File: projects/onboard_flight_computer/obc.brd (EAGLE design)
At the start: 90.2 x 95.9 mm, 191 parts, among them IC1 IS42S16160J-6BLI, IC2 S26KS512SDPBHI020, IC3 74LVC2T45GS,115, IC4 74LVCH1T45GS,132, IC5 MIMXRT1052DVJ6B, IC7 74LVCH1T45GS,132, IC8 74LVCH1T45GS,132, J1 504050-0791, J2 DX4R205JJAR1800, J3 504050-0791, J4 504050-0791, J5 504050-0791, J6 ESQ-126-37-G-D, J7 FH28-10S-0.5SH_05_, J8 504050-1091, J9 ESQ-126-37-G-D, Q1 FA-128, Q3 FC-12M, U10 HONEYWELL_HMC5983-TRHONEYWELL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, U11 HONEYWELL_HMC5983-TRHONEYWELL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, U12 HONEYWELL_HMC5983-TRHONEYWELL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, U13 DS1307N, U2 MCP1702T-1802E/CB, U3 NXP_FXAS21002CQR1NXP_FXAS2100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, U4 MK20DX128VFM5, U5 NLX2G14CMUTCG, U6 NTSX2102GU8H, U7 NXP_FXAS21002CQR1NXP_FXAS2100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, U8 NX5P3090UKZ, U9 NXP_FXAS21002CQR1NXP_FXAS2100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, Y1 ECS-.327-12.5-13X

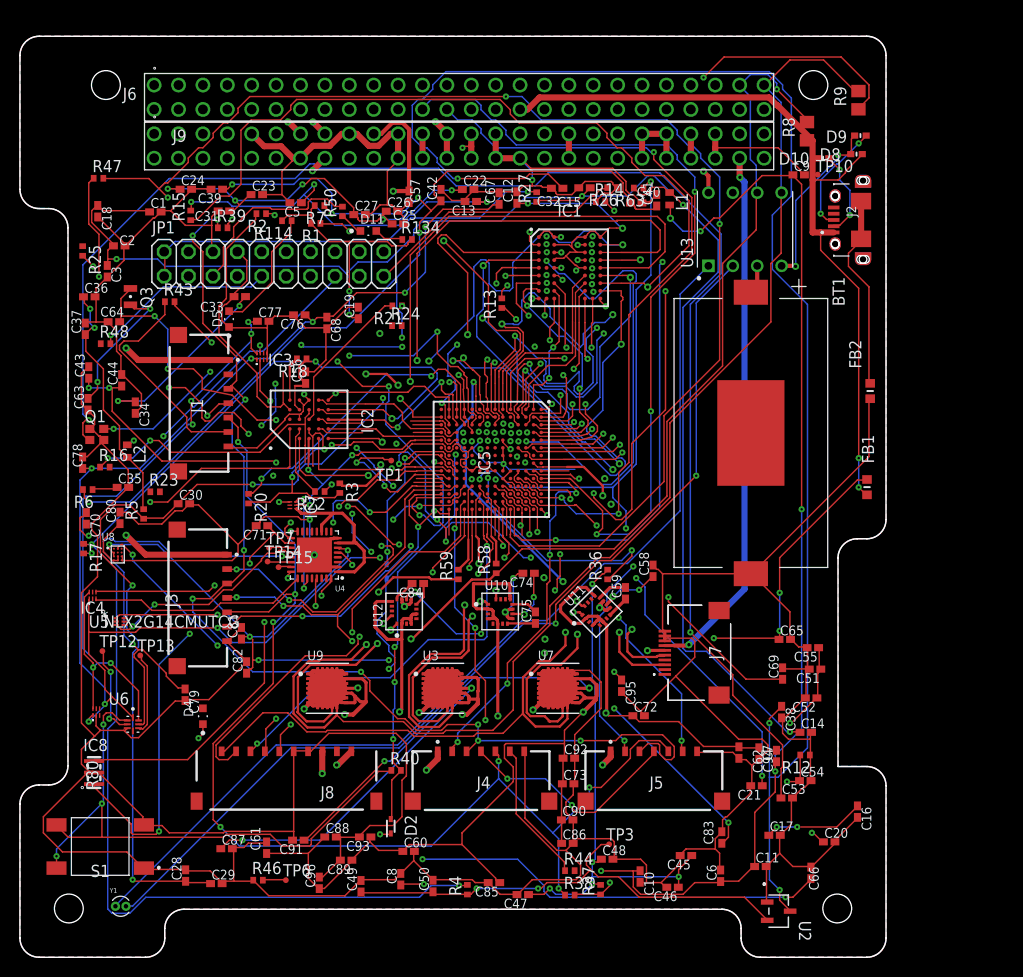
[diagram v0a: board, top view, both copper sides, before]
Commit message: RT1020 libraries added, OBC routed for RT1020
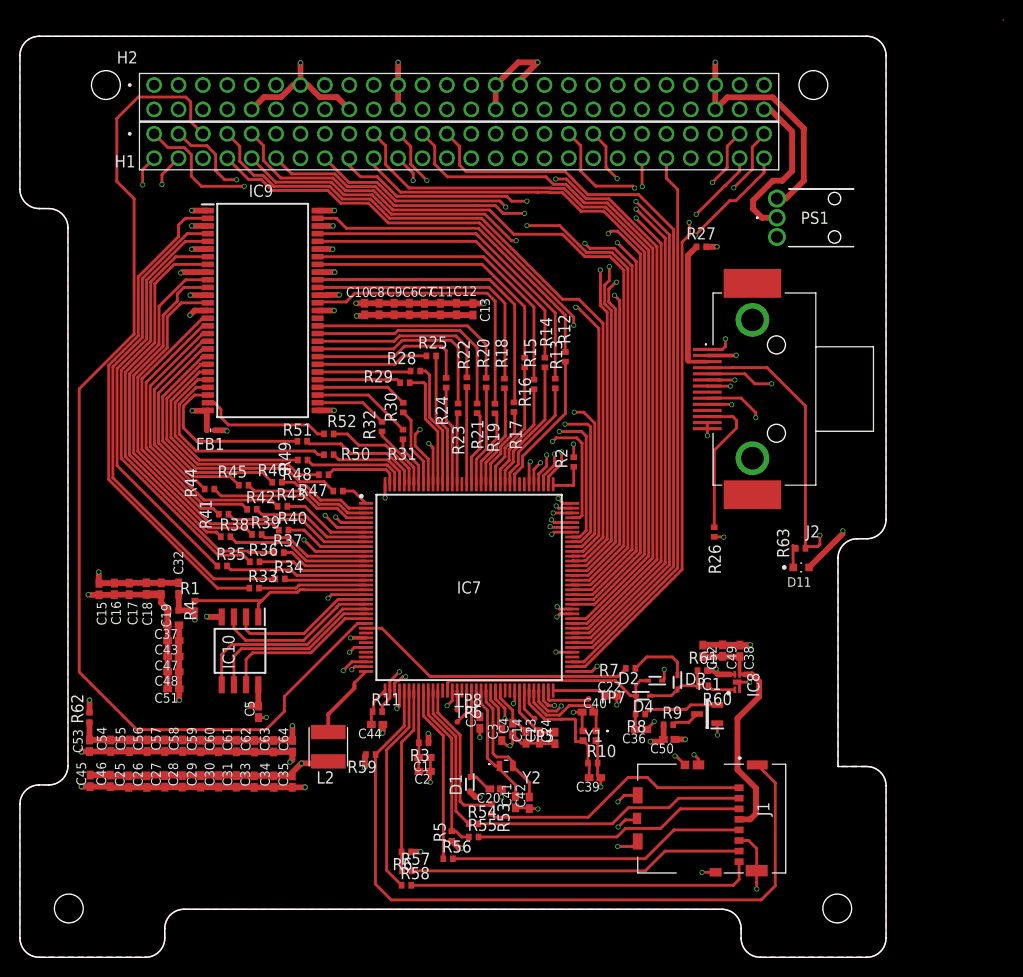
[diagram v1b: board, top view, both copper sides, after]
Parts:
- removed BT1: BA2032SM, BA2032SM:BAT_BA2032SM
- removed C65, C69, C82: 10 uF, rcl:C0402K
- removed C66: 2.2 uF, rcl:C0402K
- removed C67, C72, C73, C76, C77, C78, C81, C85, C88, C89, C92, C93, C96: 0.1 uF, rcl:C0402K
- removed C68, C86, C90, C94: 1.0 uF, rcl:C0402K
- removed C70, C71: 22 pF, rcl:C0402K
- removed C74, C80, C83: 4.7 uF, rcl:C0402K
- removed C75, C84: 0.22 uF, rcl:C0402K
- removed C79: 1000 pF, rcl:C0402K
- removed C87, C91, C95: 100 nF, rcl:C0402K
- removed D10, D8, D9: 0402ESDA-MLP1, 0402ESDA-MLP1:DIONC1105X44N
- removed D5: KINGBRIGHT_KPT-1608SGCKINGBRIGHT_KPT-1608SGC_0_0, Kingbright - KPT-1608SGC:KINGBRIGHT_KPT-1608SGC_0
- removed D6: RB521S30T1G, RB521S30T1G:SODFL1608X70N
- removed FB2: MPZ1608S331A, MPZ1608S331A:BEADC1608X95N
- removed IC2: S26KS512SDPBHI020, SDRAM_and_HyperFlash:BGA24C100P5X5_600X800X100
- removed IC3: 74LVC2T45GS,115, 74LVC2T45GS_115:74AXP2T3407GSX
- removed IC4: 74LVCH1T45GS,132, 74LVCH1T45GS_132:74LVC1G3157GS132
- removed IC5: MIMXRT1052DVJ6B, MIMXRT1052DVJ6B:BGA196C80P14X14_1200X1200X161
- removed J3, J4, J5: 504050-0791, 504050-0791:504050-0791
- removed J6, J9: ESQ-126-37-G-D, ESQ-126-37-G-D:ESQ-126-Y-X
- removed J7: FH28-10S-0.5SH_05_, FH28-10S-0.5SH_05_:FH2810S05SH05
- removed J8: 504050-1091, 504050-1091:504050-1091
- removed JP1: 20, pinhead:2X10
- removed L1: 120 Ohm, inductors:0402
- removed Q1: FA-128, crystal:FA-128
- removed Q3: FC-12M, crystal:FC-12M
- removed R114, R134: 1k Ohm, rcl:R0402
- removed R80: CSTCE8M00G55-R0, CSTCE8M00G55-R0:CSTCE12M0G55-R0
- removed S1: TL3301AF260QG, TL3301AF260QG:TL3301AF260QG
- removed TP1, TP10, TP12, TP13, TP14, TP15, TP3: TPTP06R, testpad:TP06R
- removed U10, U11, U12: HONEYWELL_HMC5983-TRHONEYWELL_HMC5983-TR_0_0, Honeywell - HMC5983-TR:HONEYWELL_HMC5983-TR_0
- removed U13: DS1307N, DS1307N:DIP762W47P254L991H457Q8
- removed U2: MCP1702T-1802E/CB, MCP1702T1802ECB:SOT-23A_MC
- removed U3, U7, U9: NXP_FXAS21002CQR1NXP_FXAS21002CQR1_0_0, NXP - FXAS21002CQR1:NXP_FXAS21002CQR1_0
- removed U4: MK20DX128VFM5, MK20DX128VFM5:QFN50P500X500X100-33N
- removed U5: NLX2G14CMUTCG, NLX2G14CMUTCG:UDFN6_1X1
- removed U6: NTSX2102GU8H, NTSX2102GU8H:QFN40P140X120X50-8N
- removed U8: NX5P3090UKZ, NX5P3090UKZ:BGA12CP40_3X4_135X165X56B26N
- added C4: 0.1uF, rcl:C0402K
- added D1, D3: BAT54XV2T1G, BAT54XV2T1G:SODFL1608X70N
- added H1, H2: ESQ-126-39-G-D, ESQ-126-39-G-D:SAMTEC_ESQ-126-39-G-D
- added IC10: IS25LP064A-JBLE, IS25LP064A-JBLE:SOIC127P790X216-8N
- added IC9: IS42S16160J-6TL, IS42S16160J-6TL:SOP80P1176X120-54N
- added PS1: PJ-040D, PJ-040D:PJ040D
- added R10: 2.2M Ohm, rcl:R0402
- added R11: 30k Ohm, rcl:R0402
- added R19, R28, R29, R30, R31, R32, R33, R34, R35, R41, R42, R45, R49, R51, R52, R53, R54, R55, R56, R57, R60, R61, R62: 0 Ohm, rcl:R0402
- added TP5, TP8: TPTP06R, testpad:TP06R
- added Y2: ECS-.327-7-12-TR, ECS-.327-7-12-TR:ECS327712TR
- C14: value 0.22uF -> 10 uF
- C16, C19, C31, C33, C48: value 4.7uF -> 0.22uF
- C17, C23, C36: value 0.22uF -> 0.1uF
- C18, C24, C35: value 0.22uF -> 4.7uF
- C2, C51: value 0.1uF -> 4.7uF
- C3: value 4.7uF -> 1.0 uF
- C32, C43: value 10uF -> 0.1uF
- C37: value 33uF -> 0.1uF
- C39: value 4.7uF -> 4.7pF
- C40: value 0.22uF -> 4.7pF
- C41, C42: value 0.22uF -> 10pF
- C44, C45, C46, C47: value 0.1uF -> 0.22uF
- C5: value 22uF -> 1.0uF
- C50: value 0.1uF -> 1.0uF
- C52: value 4.7uF -> 1.0uF
- C53, C54, C55: value 4.7uF -> 0.1uF
- C57: value 0.1 uF -> 0.1uF
- C58: value 4.7 uF -> 0.1uF
- C59: value 0.22 uF -> 0.1uF
- C60, C61, C62: value 0.1 uF -> 4.7uF
- C63, C64: value 18pF -> 4.7uF
- D2: value RB521S30T1G -> BAT54XV2T1G; device RB521S30T1G:SODFL1608X70N -> BAT54XV2T1G:SODFL1608X70N
- D4: value KINGBRIGHT_KPT-1608SGCKINGBRIGHT_KPT-1608SGC_0_0 -> BAT54XV2T1G; device Kingbright - KPT-1608SGC:KINGBRIGHT_KPT-1608SGC_0 -> BAT54XV2T1G:SODFL1608X70N
- FB1: value MPZ1608S331A -> BLM15AG121SN1D; device MPZ1608S331A:BEADC1608X95N -> BLM15AG121SN1D:NFZ15SG152SN10B
- IC1: value IS42S16160J-6BLI -> TPS3839L30DBZR; device SDRAM_and_HyperFlash:BGA54C80P9X9_800X800X120 -> TPS3839L30DBZR:SOT95P237X112-3N
- IC7: value 74LVCH1T45GS,132 -> MIMXRT1021DAG5A; device 74LVCH1T45GS_132:74LVC1G3157GS132 -> MIMXRT1021DAG5A:QFP50P2200X2200X160-144N
- IC8: value 74LVCH1T45GS,132 -> MIC94305YMT-TR; device 74LVCH1T45GS_132:74LVC1G3157GS132 -> MIC94305YMT-TR:SON50P160X120X60-5N
- J1: value 504050-0791 -> 504077-1891; device 504050-0791:504050-0791 -> 504077-1891:5040771891
- J2: value DX4R205JJAR1800 -> 12214-8250-00FR; device DX4R205JJAR1800:JAE_DX4R205JJAR1800 -> 12214-8250-00FR:12214825000FR
- L2: value 4.7 uH -> SRN4026-4R7M; device inductors:0402 -> SRN4026-4R7M:SRN4026
- R1, R5, R59: value 0 Ohm -> 10k Ohm
- R12: value 2.2M Ohm -> 0 Ohm
- R14, R15: value 100K Ohm -> 0 Ohm
- R17, R18, R3: value 10k Ohm -> 0 Ohm
- R26: value 10k Ohm -> 100 Ohm
- R36, R37: value 4.7K Ohm -> 0 Ohm
- R46: value 10K Ohm -> 0 Ohm
- R6: value 30K Ohm -> 10k Ohm
- R8: value 4.7 k -> 0 Ohm; device rcl:R0805 -> rcl:R0402
- R9: value 4.7k -> 1k Ohm; device rcl:R0805 -> rcl:R0402
- Y1: value ECS-.327-12.5-13X -> XRCGB24M000F2P01R0; device ECS-.327-12.5-13X:XTAL_ECS-.327-12.5-13X -> XRCGB24M000F2P01R0:XRCGB24M000F2P01R0
- moved C16 80.8 mm to (9.83, 38.4)
- moved C36 73.0 mm to (64.7, 23.7), turned to 180 degrees
- moved C39 72.8 mm to (59.9, 18.7)
- moved C53 72.8 mm to (7.24, 22.0), turned to 90 degrees
- moved C54 72.4 mm to (9.45, 22.0), turned to 90 degrees
- moved C17 71.9 mm to (11.4, 38.4), turned to 270 degrees
- moved C55 71.9 mm to (11.4, 22.0), turned to 90 degrees
- moved C24 68.8 mm to (55.7, 22.8), turned to 90 degrees
- moved FB1 68.6 mm to (19.9, 54.9), turned to 180 degrees
- moved R9 68.0 mm to (67.5, 24.2), turned to 0 degrees
- moved C6 67.3 mm to (40.5, 67.5)
- moved C11 66.9 mm to (43.8, 67.5), turned to 90 degrees
- moved C51 66.8 mm to (16.0, 27.9)
- moved IC8 66.8 mm to (74.7, 28.7), turned to 90 degrees
- moved J1 66.1 mm to (72.0, 14.8), turned to 270 degrees
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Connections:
- removed net 12V_BUS: J9.23, J9.24
- removed net 12V_PDM1: J9.8
- removed net 12V_PDM2: J9.10
- removed net 3V3_PDM10: J9.20
- removed net 3V3_PDM8: J9.18
- removed net 3V3_PDM9: C57.1, C60.1, C61.1, C62.1, C72.1, C73.1, C85.1, C86.1, C88.1, C89.1, C90.1, C92.1, C93.1, C94.1, C96.1, J7.6, J9.19, U10.13, U10.2, U10.4, U10.6, U11.13, U11.2, U11.4, U11.6, U12.13, U12.2, U12.4, U12.6, U3.13, U3.15, U3.17, U3.18, U7.13, U7.15, U7.17, U7.18, U9.13, U9.15, U9.17, U9.18
- removed net 5V_BUS: J9.25, J9.26, R8.1, R9.1, U13.8
- removed net 5V_PDM5: J8.3, J9.13
- removed net 5V_PDM6: J1.1, J3.1, J4.1, J5.1, J9.15
- removed net 5V_PDM7: J8.1, J9.16
- removed net 5V_USB_CHARGE: D8.2, FB1.1, J2.1, J6.32
- removed net AAA: U8.A1
- removed net BATV_BUS: J9.45, J9.46
- removed net BATV_PDM3: J9.11
- removed net BATV_PDM4: J9.12
- removed net BCR_OUT: J9.41, J9.42, J9.43, J9.44
- removed net CAN_STBY: IC5.G14, R44.2
- removed net CHASSIS: J7.7, J9.50
- removed net DCDC_3V3: C1.1, C14.1, C15.1, C18.1, C19.1, C2.1, C3.1, D6.2, IC5.E6, IC5.F5, IC5.N14, IC5.P12, L1.1, R1.2, R114.2, R134.2, R27.1, R63.2, R7.2
- removed net FLASH_RST: IC5.D7, R2.1
- removed net FLASH_VCC: C51.1, C52.1, C55.1, C56.1, IC2.B4, IC2.D1, IC2.E4, IC5.K5, R17.1, R18.1, R3.1, R4.2
- removed net FLEXSPI_CLK_B: IC2.B1, IC5.P2
- removed net FLEXSPI_D0_B: IC2.D5, IC5.M4
- removed net FLEXSPI_D1_B: IC2.E3, IC5.M3
- removed net FLEXSPI_D2_B: IC2.E2, IC5.M5
- removed net FLEXSPI_D3_B: IC2.E1, IC5.L5
- removed net FLEXSPI_DQS: IC5.N3, R21.1
- removed net GPIO_AD_B1_00: IC5.J11, R58.2
- removed net GPIO_AD_B1_01: IC5.K11, R59.2
- removed net LDO_1V8: C49.1, C50.1, R4.1, TP3.TP, U2.2
- removed net MCU_DCDC_IN: C39.1, C40.1, C41.1, C42.1, IC5.K4, IC5.L1, IC5.L2, R6.2, R7.1
- removed net N$27: IC2.A5, R18.2
- removed net N$29: IC2.A4, R2.2
- removed net N$31: IC2.C2, R20.2, R3.2
- removed net N$34: IC2.B2, R22.2
- removed net N$37: JP1.19, R26.2
- removed net N$39: D2.1, JP1.15
- removed net N$40: C32.1, C38.1, R1.1, U2.3
- removed net N$46: C75.1, U10.8
- removed net N$48: C59.1, U11.8
- removed net N$49: C84.2, U12.12
- removed net N$53: C63.2, IC5.N9, Q3.2
- removed net N$54: U6.5
- removed net N$56: C83.1, U12.10
- removed net N$57: TP12.TP, U6.3
- removed net N$60: TP13.TP, U6.6
- removed net N$67: C91.1, U7.16
- removed net N$71: C87.1, U3.16
- removed net N$72: C95.1, U9.16
- removed net N$76: D11.2, R134.1
- removed net P3V3_SDA: C67.1, C68.1, C69.1, C76.1, C78.1, IC3.1, IC4.1, IC7.1, IC8.1, U4.1, U4.11, U4.7, U5.5, U6.1
- removed net P5V_SDA: C65.1, C81.1, C82.1, FB1.2, U4.6, U8.B1, U8.B2, U8.C1
- removed net P5V_SDA_S: C80.1, U8.C2, U8.D1, U8.D2
- removed net PCM_IN: J9.35, J9.36
- removed net POWER_EN: U4.31
- removed net POWER_LED: D5.2, R114.1
- removed net SDA_EXTAL: C70.1, R80.3, U4.17
- removed net SDA_LED: D4.1, U4.29
- removed net SDA_RST: TP7.TP, U4.19
- removed net SDA_RST_TGTMCU_B: C79.1, R40.1, S1.2, S1.4, U4.21, U6.2, U6.7
- removed net SDA_RX_EN: IC4.5
- removed net SDA_SPI0_CS: TP15.TP, U4.23
- removed net SDA_SPI0_RST_B: TP14.TP, U4.22
- removed net SDA_SPI0_SCK: IC8.3, U4.26
- removed net SDA_SPI0_SIN: IC3.3, U4.28
- removed net SDA_SPI0_SOUT: IC7.3, U4.27
- removed net SDA_SWD_EN: IC8.5, U5.6
- removed net SDA_SWD_EN_B: U4.16, U5.1
- removed net SDA_SWD_OE: IC7.5, U5.4
- removed net SDA_SWD_OE_B: U4.20, U5.3
- removed net SDA_USBSHIELD: FB2.2, J2.S4, J2.S5
- removed net SDA_USB_CONN_DN: D10.2, J2.2
- removed net SDA_USB_CONN_DP: D9.2, J2.3
- removed net SDA_USB_DN: U4.4
- removed net SDA_USB_DP: U4.3
- removed net SDA_VOUT33: C66.1, U4.5
- removed net SDA_XTAL: C71.1, R80.1, U4.18
- removed net SPI1_EN_1: IC5.A9, J1.2
- removed net SPI1_EN_2: IC5.B9, J3.2
- removed net SPI1_EN_3: IC5.C9, J4.2
- removed net SPI1_EN_4: IC5.D9, J5.2
- removed net SPI1_NSS_1: J1.6, R43.1
- removed net SPI1_NSS_2: IC5.F11, J3.6
- removed net SPI1_NSS_3: J4.6, R44.1
- removed net SPI1_NSS_4: IC5.H14, J5.6
- removed net SWD_CLK: IC8.4, R48.1
- removed net SWD_DIO: IC3.6, IC7.4, R47.1
- removed net TC_SDA_USB_ID_TP: J2.4, TP10.TP
- removed net UART1_RXD: IC4.4, IC5.L14
- removed net UART1_RX_TGTMCU_R: IC4.3, U4.25
- removed net UART1_TXD: IC3.7, IC5.K14
- removed net UART1_TX_TGTMCU_R: IC3.2, U4.24
- removed net UART2_RX: IC5.M12, J6.3
- removed net UART2_TX: IC5.L11, J6.1
- removed net UART8_RX: IC5.J13, J8.8
- removed net UART8_TX: IC5.L13, J8.7
- removed net USB_OTG1_ID: IC5.H10, R36.1, R39.2
- removed net USB_OTG1_OC: IC5.G11, R43.2
- removed net VDD_SOC_IN: C22.1, C23.1, C24.1, C25.1, C26.1, C27.1, C28.1, C29.1, C30.1, C31.1, IC5.F6, IC5.F7, IC5.F8, IC5.F9, IC5.J5, R5.1
- removed net VTRG_FAULT_B: U4.32, U8.A2
- removed net V_TGTMCU: C77.1, IC3.8, IC4.6, IC7.6, IC8.6, U6.8
- new net 5V_USB: H2.52, PS1.1
- new net 5V_USB_OTG: C3.2, IC7.59
- new net FLASH_3V3: C32.2, C5.2, IC10.8, R1.1, R4.2
- new net GPANAIO: IC7.71, TP7.TP
- new net GPIO_EMC_16: IC9.23, R49.1
- new net GPIO_EMC_17: IC9.24, R50.1
- new net GPIO_EMC_18: IC9.25, R51.1
- new net GPIO_EMC_19: IC9.26, R52.1
- new net GPIO_EMC_20: IC9.29, R32.2
- new net GPIO_EMC_21: IC9.30, R31.2
- new net GPIO_EMC_22: IC9.31, R30.2
- new net GPIO_EMC_23: IC9.32, R29.2
- new net GPIO_EMC_24: IC9.33, R28.2
- new net GPIO_EMC_25: IC9.34, R25.2
- new net GPIO_EMC_26: IC9.35, R24.2
- new net GPIO_EMC_27: IC9.36, R23.2
- new net INT1_COMBO: IC7.27, R7.1
- new net JTAG_DACK: J2.13, R26.1
- new net JTAG_NSRST: D2.1, J2.12
- new net N$12: IC9.11, R39.1
- new net N$14: IC9.13, R40.1
- new net N$15: J1.5, R56.2
- new net N$16: IC9.15, R41.1
- new net N$17: IC9.16, R42.1
- new net N$18: IC9.17, R43.1
- new net N$19: IC9.18, R44.1
- new net N$20: IC9.19, R45.1
- new net N$21: IC9.20, R46.1
- new net N$22: IC9.21, R47.1
- new net N$23: IC9.22, R48.1
- new net N$24: D3.2, D4.2, R60.1, R61.1
- new net N$25: J1.7, R57.2
- new net N$42: IC9.47, R16.2
- new net NVCC_PLL: C22.2, IC7.72
- new net NVCC_SD0: C1.2, C2.2, IC7.44, R3.2
- new net PMIC_STBY_REQ: IC7.54, TP6.TP
- new net RTC_XTALI: C41.2, IC7.57, Y2.1
- new net SD1_CLK: IC7.45, R56.1
- new net SD1_CMD: IC7.46, R5.2, R55.1
- new net SD1_D0: IC7.43, R57.1, R6.2
- new net SD1_D1: IC7.42, R58.1
- new net SD1_D2: IC7.48, R53.1
- new net SD1_D3: IC7.47, R54.1
- new net SD_CD_SW: IC7.41, J1.9, R59.1
- new net SD_PWREN: D3.1, R7.2
- new net SPI1_EN0: H1.9, IC7.92
- new net SPI1_EN1: H1.10, IC7.91
- new net SPI1_EN2: H1.22, IC7.90
- new net SPI1_EN3: H1.21, IC7.89
- new net SPI1_PCS0: H1.7, IC7.97
- new net SPI1_PCS1: H1.8, IC7.88
- new net SPI1_PCS2: H1.20, IC7.87
- new net SPI1_PCS3: H1.19, IC7.84
- new net UART1_RX: H1.4, IC7.101
- new net UART1_TX: H1.2, IC7.105
- new net UART4_RX: H1.3, IC7.79
- new net UART4_TX: H1.1, IC7.80
- new net USB_OTG1_CHD: IC7.66, TP5.TP
- new net VDD_HIGH_CAP: C23.2, C24.2, IC7.65
- new net VDD_SNVS_CAP: C21.2, IC7.56
- new net VSD_3V3: C38.2, C49.2, C52.2, IC8.3, J1.4
- new net WAKEUP: IC7.52, TP8.TP
- new net XTALO: C40.2, IC7.68, Y1.1
- net 3V3_BUS: now also C15.2, C16.2, C17.2, C18.2, C19.2, C37.2, C43.2, C47.2, C48.2, C50.2, C51.2, D1.2, D11.2, FB1.1, H2.27, H2.28, IC7.34, IC7.38, IC7.69, IC7.73, IC8.4, J2.8, R11.2, R27.2, R3.1, R4.1, R5.1, R59.2, R6.1, R61.2, R62.2, R9.1; no longer IC5.J6, J9.27, J9.28
- net ANT_BURN_WIRE1: now also H1.23, IC7.83; no longer IC5.A10, J6.24
- net ANT_BURN_WIRE2: now also H1.25, IC7.78; no longer IC5.D10, J6.26
- net DCDC_OUT: now also C25.2, C26.2, C27.2, C28.2, C29.2, C30.2, C31.2, C33.2, C34.2, C35.2, C45.2, C46.2, IC7.102, IC7.114, IC7.134, IC7.31, IC7.39, IC7.5, IC7.86, L2.1; no longer C36.1, C37.1, L2.2, R5.2
- net DTR: now also H1.5, IC7.26; no longer IC5.C10, J8.6
- net FLEXSPI_CLK: now also IC10.6, IC7.24; no longer IC5.L4, R22.1
- net FLEXSPI_D0_A: now also IC10.5, IC7.23; no longer IC5.P3, R24.2
- net FLEXSPI_D1_A: now also IC10.2, IC7.21; no longer IC5.N4, R23.2
- net FLEXSPI_D2_A: now also IC10.3, IC7.22; no longer IC5.P4, R16.2
- net FLEXSPI_D3_A: now also IC10.7, IC7.25; no longer IC5.P5, R25.2
- net FLEXSPI_SS0: now also IC10.1, IC7.19, R1.2; no longer IC5.L3, R20.1
- net GND: now also C1.1, C14.1, C15.1, C16.1, C17.1, C18.1, C19.1, C2.1, C20.1, C21.1, C22.1, C23.1, C24.1, C25.1, C26.1, C27.1, C28.1, C29.1, C3.1, C30.1, C31.1, C32.1, C33.1, C34.1, C35.1, C36.1, C37.1, C38.1, C39.1, C4.1, C40.1, C41.1, C42.1, C43.1, C44.1, C45.1, C46.1, C47.1, C48.1, C49.1, C5.1, C50.1, C51.1, C52.1, C53.1, C54.1, C55.1, C56.1, C57.1, C58.1, C59.1, C60.1, C61.1, C62.1, H2.10, H2.13, H2.18, H2.21, H2.22, H2.29, H2.30, H2.31, H2.47, H2.48, IC1.1, IC10.4, IC7.103, IC7.113, IC7.135, IC7.35, IC7.40, IC7.51, IC7.6, IC7.60, IC7.64, IC7.70, IC7.85, IC8.5, IC9.12, IC9.28, IC9.41, IC9.46, IC9.52, IC9.54, IC9.6, J1.10, J1.11, J1.12, J1.13, J1.14, J1.15, J1.16, J1.6, J2.1, J2.14, J2.7, PS1.2, R10.2, R2.1, R26.2, Y1.2, Y1.4; no longer BT1.-, C1.2, C14.2, C15.2, C16.2, C17.2, C18.2, C19.2, C2.2, C20.2, C21.2, C22.2, C23.2, C24.2, C25.2, C26.2, C27.2, C28.2, C29.2, C3.2, C30.2, C31.2, C32.2, C33.2, C34.2, C35.2, C36.2, C37.2, C38.2, C39.2, C40.2, C41.2, C42.2, C43.2, C44.2, C45.2, C46.2, C47.2, C48.2, C49.2, C5.2, C50.2, C51.2, C52.2, C53.2, C54.2, C55.2, C56.2, C57.2, C58.2, C60.2, C61.2, C62.2, C65.2, C66.2, C67.2, C68.2, C69.2, C70.2, C71.2, C72.2, C73.2, C74.2, C76.2, C77.2, C78.2, C79.2, C80.2, C81.2, C82.2, C83.2, C85.2, C86.2, C87.2, C88.2, C89.2, C90.2, C91.2, C92.2, C93.2, C94.2, C95.2, C96.2, D10.1, D5.1, D8.1, D9.1, FB2.1, IC1.A1, IC1.A3, IC1.B7, IC1.C3, IC1.D7, IC1.E3, IC1.J1, IC2.B3, IC2.B5, IC2.C1, IC2.C5, IC2.E5, IC3.4, IC3.5, IC4.2, IC5.A1, IC5.A14, IC5.G9, IC5.K6, IC5.K9, IC5.N1, IC5.N2, IC7.2, J1.7, J2.5, J3.7, J4.7, J5.7, J7.10, J7.8, J7.9, J8.4, J8.5, J9.14, J9.17, J9.21, J9.22, J9.29, J9.30, J9.32, J9.47, J9.48, J9.9, JP1.10, JP1.12, JP1.14, JP1.16, JP1.18, JP1.20, JP1.4, JP1.6, JP1.8, Q1.2, Q1.4, R12.1, R14.1, R26.1, R46.1, R80.2, S1.1, S1.3, U10.11, U10.9, U11.11, U11.9, U12.11, U12.9, U13.4, U2.1, U3.1, U3.10, U3.14, U3.19, U3.20, U3.21, U3.22, U3.23, U3.24, U3.5, U3.6, U3.7, U3.8, U3.9, U4.2, U4.33, U4.8, U5.2, U6.4, U7.1, U7.10, U7.14, U7.19, U7.20, U7.21, U7.22, U7.23, U7.24, U7.5, U7.6, U7.7, U7.8, U7.9, U8.B3, U8.C3, U8.D3, U9.1, U9.10, U9.14, U9.19, U9.20, U9.21, U9.22, U9.23, U9.24, U9.5, U9.6, U9.7, U9.8, U9.9
- net I2C1_SCL: now also H1.44, IC7.75; no longer J6.49, R58.1, R8.2, U12.1, U13.6, U9.11
- net I2C1_SDA: now also H1.42, IC7.74; no longer J6.51, R59.1, R9.2, U12.16, U13.5, U9.12
- net I2C2_SCL: now also H1.37, IC7.82; no longer IC5.C8, U10.1, U3.11
- net I2C2_SDA: now also H1.35, IC7.81; no longer IC5.B8, U10.16, U3.12
- net I2C3_SCL: now also H1.51, IC7.100; no longer IC5.J4, J8.9, U11.1, U7.11
- net I2C3_SDA: now also H1.49, IC7.99; no longer IC5.J3, J8.10, U11.16, U7.12
- net JTAG_DE: now also J2.6; no longer JP1.17
- net JTAG_MOD: now also IC7.109, R2.2; no longer IC5.F13, R46.2, TP6.TP
- net JTAG_NTRST: now also IC7.106, J2.9, R63.2; no longer IC5.G10, JP1.3
- net JTAG_RTCK: now also J2.11; no longer JP1.11
- net JTAG_TCK: now also IC7.110, J2.4; no longer IC5.F12, JP1.9, R48.2
- net JTAG_TDI: now also IC7.108, J2.3; no longer IC5.F14, JP1.5, R50.2
- net JTAG_TDO: now also IC7.107, J2.5; no longer IC5.G13, JP1.13
- net JTAG_TMS: now also IC7.111, J2.10; no longer IC5.E14, JP1.7, R47.2
- net N$1: now also IC1.2, R8.1; no longer D4.2
- net N$10: now also J1.3, R55.2; no longer IC5.M14, R37.1, R38.2
- net N$11: now also IC9.10, R38.1; no longer C53.1, IC5.N11, Q1.1
- net N$13: now also IC8.1, R60.2; no longer IC1.F2, R13.2
- net N$2: now also IC9.2, R33.1; no longer C16.1, C17.1, IC5.P8
- net N$26: now also J1.8, R58.2; no longer IC2.C4, R16.1
- net N$3: now also IC1.3, R9.2; no longer C20.1, IC5.M10
- net N$30: now also IC9.53, R12.2; no longer U13.2, Y1.2
- net N$32: now also IC9.51, R13.2; no longer IC2.C3, R21.2
- net N$33: now also IC9.50, R14.2; no longer IC2.D2, R23.1
- net N$35: now also IC9.48, R15.2; no longer IC2.D3, R24.1
- net N$36: now also IC7.36, L2.2; no longer IC2.D4, R25.1
- net N$38: now also J2.2, R27.1; no longer JP1.1, JP1.2, R27.2
- net N$4: now also J1.1, R53.2; no longer C35.1, IC5.K3, R6.1
- net N$41: now also C44.2, IC7.37, R11.1; no longer U13.1, Y1.1
- net N$44: now also IC9.45, R17.2; no longer BT1.+, U13.3
- net N$45: now also IC9.44, R18.2; no longer C75.2, U10.12
- net N$47: now also IC9.42, R19.2; no longer C59.2, U11.12
- net N$5: now also IC9.4, R34.1; no longer C21.1, D6.1, IC5.M9
- net N$50: now also IC9.39, R20.2; no longer C84.1, U12.8
- net N$51: now also IC9.38, R21.2; no longer C58.1, U11.10
- net N$52: now also IC9.37, R22.2; no longer C74.1, U10.10
- net N$59: now also C20.2, D1.1, IC7.55; no longer U8.A3
- net N$6: now also IC9.5, R35.1; no longer IC5.M1, IC5.M2, L2.1
- net N$7: now also J1.2, R54.2; no longer C33.1, C34.1, IC5.P10
- net N$8: now also IC9.7, R36.1; no longer IC2.A2, R17.2
- net N$9: now also IC9.8, R37.1; no longer IC5.N10, TP1.TP
- net NVCC_GPIO_3V3: now also C53.2, C54.2, C55.2, C56.2, C57.2, C58.2, C59.2, C60.2, C61.2, C62.2, C63.2, C64.2, IC7.104, IC7.11, IC7.112, IC7.144, IC7.20, IC7.29, IC7.77, R62.1; no longer C45.1, C46.1, C47.1, C48.1, IC5.E9, IC5.F10, IC5.J10, R36.2, R37.2, R63.1
- net POR_B: now also C36.2, D4.1, IC7.50, R8.2; no longer IC5.M7, R40.2
- net RTC_XTALO: now also C42.2, IC7.58, Y2.2; no longer C64.2, IC5.P9, Q3.1
- net SDRAM_3V3: now also FB1.2, IC9.1, IC9.14, IC9.27, IC9.3, IC9.43, IC9.49, IC9.9; no longer C5.1, IC1.A7, IC1.A9, IC1.B3, IC1.C7, IC1.D3, IC1.E7, IC1.J9, L1.2, R15.2
- net SEMC_A0: now also IC7.142, R49.2; no longer IC1.H7, IC5.C2
- net SEMC_A1: now also IC7.141, R50.2; no longer IC1.H8, IC5.G1
- net SEMC_A10: now also IC7.143, R48.2; no longer IC1.H9, IC5.G2
- net SEMC_A11: now also IC7.130, R24.1; no longer IC1.G2, IC5.B4
- net SEMC_A12: now also IC7.129, R23.1; no longer IC1.G1, IC5.A3
- net SEMC_A2: now also IC7.140, R51.2; no longer IC1.J8, IC5.G3
- net SEMC_A3: now also IC7.139, R52.2; no longer IC1.J7, IC5.H1
- net SEMC_A4: now also IC7.138, R32.1; no longer IC1.J3, IC5.A6
- net SEMC_A5: now also IC7.137, R31.1; no longer IC1.J2, IC5.B6
- net SEMC_A6: now also IC7.136, R30.1; no longer IC1.H3, IC5.B1
- net SEMC_A7: now also IC7.133, R29.1; no longer IC1.H2, IC5.A5
- net SEMC_A8: now also IC7.132, R28.1; no longer IC1.H1, IC5.A4
- net SEMC_A9: now also IC7.131, R25.1; no longer IC1.G3, IC5.B2
- net SEMC_BA0: now also IC7.2, R46.2; no longer IC1.G7, IC5.C1
- net SEMC_BA1: now also IC7.1, R47.2; no longer IC1.G8, IC5.F1
- net SEMC_CAS: now also IC7.7, R43.2; no longer IC1.F7, IC5.D3
- net SEMC_CKE: now also IC7.127, R22.1; no longer IC1.F3, IC5.A2, R14.2
- net SEMC_CLK: now also IC7.126, R21.1; no longer IC5.B3, R13.1
- net SEMC_CS0: now also IC7.3, R45.2; no longer IC1.G9, IC5.E1, R15.1
- net SEMC_D0: now also IC7.18, R33.2; no longer IC1.A8, IC5.E3
- net SEMC_D1: now also IC7.17, R34.2; no longer IC1.B9, IC5.F3
- net SEMC_D10: now also IC7.122, R17.1; no longer IC1.D1, IC5.D5
- net SEMC_D11: now also IC7.121, R16.1; no longer IC1.C2, IC5.C4
- net SEMC_D12: now also IC7.120, R15.1; no longer IC1.C1, IC5.D4
- net SEMC_D13: now also IC7.119, R14.1; no longer IC1.B2, IC5.E5
- net SEMC_D14: now also IC7.118, R13.1; no longer IC1.B1, IC5.C3
- net SEMC_D15: now also IC7.117, R12.1; no longer IC1.A2, IC5.E4
- net SEMC_D2: now also IC7.16, R35.2; no longer IC1.B8, IC5.F4
- net SEMC_D3: now also IC7.15, R36.2; no longer IC1.C9, IC5.G4
- net SEMC_D4: now also IC7.14, R37.2; no longer IC1.C8, IC5.F2
- net SEMC_D5: now also IC7.13, R38.2; no longer IC1.D9, IC5.G5
- net SEMC_D6: now also IC7.12, R39.2; no longer IC1.D8, IC5.H5
- net SEMC_D7: now also IC7.10, R40.2; no longer IC1.E9, IC5.H4
- net SEMC_D8: now also IC7.124, R19.1; no longer IC1.E1, IC5.C6
- net SEMC_D9: now also IC7.123, R18.1; no longer IC1.D2, IC5.C5
- net SEMC_DM0: now also IC7.9, R41.2; no longer IC1.E8, IC5.H3
- net SEMC_DM1: now also IC7.125, R20.1; no longer IC1.F1, IC5.D6
- net SEMC_RAS: now also IC7.4, R44.2; no longer IC1.F8, IC5.D2
- net SEMC_WE: now also IC7.8, R42.2; no longer IC1.F9, IC5.D1
- net SPI1_MISO: now also H1.18, IC7.95; no longer IC5.M11, J1.4, J3.4, J4.4, J5.4
- net SPI1_MOSI: now also H1.16, IC7.96; no longer J1.3, J3.3, J4.3, J5.3, R39.1
- net SPI1_SCK: now also H1.12, IC7.98; no longer J1.5, J3.5, J4.5, J5.5, R38.1
- net UART3_RX: now also H1.52, IC7.93; no longer IC5.K10, J7.5
- net UART3_TX: now also H1.50, IC7.94; no longer IC5.J12, J7.3
- net USER_LED: now also R63.1; no longer R50.1
- net VDD_USB_3V: now also C14.2, C4.2, IC7.61; no longer C43.1, C44.1, IC5.K8
- net XTALI: now also C39.2, IC7.67, R10.1, Y1.3; no longer C54.1, IC5.P11, Q1.3, R12.2
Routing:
- net GND: track 829.9 -> 236.1 mm, vias 25 -> 57
- net 3V3_BUS: track 62.3 -> 486.1 mm, vias 3 -> 17
- net 3V3_PDM9: track 341.1 -> 0.00 mm, vias 8 -> 0
- net DCDC_3V3: track 285.2 -> 0.00 mm, vias 10 -> 0
- net FLASH_VCC: track 228.5 -> 0.00 mm, vias 7 -> 0
- net P3V3_SDA: track 206.9 -> 0.00 mm, vias 10 -> 0
- net N$40: track 179.3 -> 0.00 mm, vias 4 -> 0
- net VDD_SOC_IN: track 177.4 -> 0.00 mm, vias 11 -> 0
- net 5V_PDM6: track 171.9 -> 0.00 mm, vias 5 -> 0
- net XTALI: track 151.3 -> 14.2 mm, vias 5 -> 0
- net MCU_DCDC_IN: track 131.1 -> 0.00 mm, vias 7 -> 0
- net N$11: track 162.2 -> 36.0 mm, vias 2 -> 0
- net SDA_RST_TGTMCU_B: track 122.6 -> 0.00 mm, vias 5 -> 0
- net P5V_SDA: track 117.6 -> 0.00 mm, vias 8 -> 0
- net JTAG_TMS: track 142.8 -> 28.8 mm, vias 3 -> 2
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
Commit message: new OBC files
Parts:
- added R64, R65, R66, R67: 0 Ohm, rcl:R0402
- C52: value 1.0uF -> 4.7uF
- moved C45 46.5 mm to (50.4, 35.8), flipped to the bottom
- moved C27 46.4 mm to (51.0, 47.7), flipped to the bottom, turned to 180 degrees
- moved C57 44.8 mm to (53.6, 44.9), flipped to the bottom, turned to 180 degrees
- moved R62 43.2 mm to (50.1, 30.5), flipped to the bottom, turned to 180 degrees
- moved C29 43.2 mm to (54.2, 43.1), flipped to the bottom
- moved C55 42.9 mm to (52.9, 32.8), flipped to the bottom, turned to 270 degrees
- moved C26 42.9 mm to (45.7, 46.3), flipped to the bottom
- moved C28 42.6 mm to (51.6, 43.1), flipped to the bottom
- moved C54 42.6 mm to (50.7, 32.8), flipped to the bottom, turned to 270 degrees
- moved C25 42.3 mm to (43.0, 46.3), flipped to the bottom
- moved C53 41.3 mm to (39.7, 47.6), flipped to the bottom, turned to 0 degrees
- moved C46 39.2 mm to (38.6, 44.6), flipped to the bottom
- moved C51 39.0 mm to (55.0, 29.9), flipped to the bottom, turned to 90 degrees
- moved C48 36.7 mm to (52.7, 29.9), flipped to the bottom, turned to 90 degrees
- moved C31 36.7 mm to (54.7, 35.8), flipped to the bottom
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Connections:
- removed net FLASH_3V3: C32.2, C5.2, IC10.8, R1.1, R4.2
- removed net GPIO_EMC_16: IC9.23, R49.1
- removed net GPIO_EMC_17: IC9.24, R50.1
- removed net GPIO_EMC_18: IC9.25, R51.1
- removed net GPIO_EMC_19: IC9.26, R52.1
- removed net GPIO_EMC_20: IC9.29, R32.2
- removed net GPIO_EMC_21: IC9.30, R31.2
- removed net GPIO_EMC_22: IC9.31, R30.2
- removed net GPIO_EMC_23: IC9.32, R29.2
- removed net GPIO_EMC_24: IC9.33, R28.2
- removed net GPIO_EMC_25: IC9.34, R25.2
- removed net GPIO_EMC_26: IC9.35, R24.2
- removed net GPIO_EMC_27: IC9.36, R23.2
- removed net INT1_COMBO: IC7.27, R7.1
- removed net N$1: IC1.2, R8.1
- removed net N$10: J1.3, R55.2
- removed net N$11: IC9.10, R38.1
- removed net N$12: IC9.11, R39.1
- removed net N$13: IC8.1, R60.2
- removed net N$14: IC9.13, R40.1
- removed net N$15: J1.5, R56.2
- removed net N$16: IC9.15, R41.1
- removed net N$17: IC9.16, R42.1
- removed net N$18: IC9.17, R43.1
- removed net N$19: IC9.18, R44.1
- removed net N$2: IC9.2, R33.1
- removed net N$20: IC9.19, R45.1
- removed net N$21: IC9.20, R46.1
- removed net N$22: IC9.21, R47.1
- removed net N$23: IC9.22, R48.1
- removed net N$24: D3.2, D4.2, R60.1, R61.1
- removed net N$25: J1.7, R57.2
- removed net N$26: J1.8, R58.2
- removed net N$30: IC9.53, R12.2
- removed net N$32: IC9.51, R13.2
- removed net N$33: IC9.50, R14.2
- removed net N$35: IC9.48, R15.2
- removed net N$4: J1.1, R53.2
- removed net N$42: IC9.47, R16.2
- removed net N$44: IC9.45, R17.2
- removed net N$45: IC9.44, R18.2
- removed net N$47: IC9.42, R19.2
- removed net N$5: IC9.4, R34.1
- removed net N$50: IC9.39, R20.2
- removed net N$51: IC9.38, R21.2
- removed net N$52: IC9.37, R22.2
- removed net N$6: IC9.5, R35.1
- removed net N$7: J1.2, R54.2
- removed net N$8: IC9.7, R36.1
- removed net N$9: IC9.8, R37.1
- removed net NVCC_GPIO_3V3: C53.2, C54.2, C55.2, C56.2, C57.2, C58.2, C59.2, C60.2, C61.2, C62.2, C63.2, C64.2, IC7.104, IC7.11, IC7.112, IC7.144, IC7.20, IC7.29, IC7.77, R62.1
- removed net NVCC_SD0: C1.2, C2.2, IC7.44, R3.2
- new net CHASSIS: R64.2, R65.2, R66.2, R67.2
- net 3V3_BUS: now also C1.2, C2.2, C32.2, C5.2, C53.2, C54.2, C55.2, C56.2, C57.2, C58.2, C59.2, C60.2, C61.2, C62.2, C63.2, C64.2, D3.2, D4.2, IC10.8, IC7.104, IC7.11, IC7.112, IC7.144, IC7.20, IC7.29, IC7.44, IC7.77, IC8.1, R1.1, R3.2, R4.2, R60.1, R60.2, R61.1, R62.1
- net GND: now also R64.1, R65.1, R66.1, R67.1
- net POR_B: now also IC1.2, R8.1
- net SD1_CLK: now also J1.5, R56.2
- net SD1_CMD: now also J1.3, R55.2
- net SD1_D0: now also J1.7, R57.2
- net SD1_D1: now also J1.8, R58.2
- net SD1_D2: now also J1.1, R53.2
- net SD1_D3: now also J1.2, R54.2
- net SD_PWREN: now also IC7.27, R7.1
- net SEMC_A0: now also IC9.23, R49.1
- net SEMC_A1: now also IC9.24, R50.1
- net SEMC_A10: now also IC9.22, R48.1
- net SEMC_A11: now also IC9.35, R24.2
- net SEMC_A12: now also IC9.36, R23.2
- net SEMC_A2: now also IC9.25, R51.1
- net SEMC_A3: now also IC9.26, R52.1
- net SEMC_A4: now also IC9.29, R32.2
- net SEMC_A5: now also IC9.30, R31.2
- net SEMC_A6: now also IC9.31, R30.2
- net SEMC_A7: now also IC9.32, R29.2
- net SEMC_A8: now also IC9.33, R28.2
- net SEMC_A9: now also IC9.34, R25.2
- net SEMC_BA0: now also IC9.20, R46.1
- net SEMC_BA1: now also IC9.21, R47.1
- net SEMC_CAS: now also IC9.17, R43.1
- net SEMC_CKE: now also IC9.37, R22.2
- net SEMC_CLK: now also IC9.38, R21.2
- net SEMC_CS0: now also IC9.19, R45.1
- net SEMC_D0: now also IC9.2, R33.1
- net SEMC_D1: now also IC9.4, R34.1
- net SEMC_D10: now also IC9.45, R17.2
- net SEMC_D11: now also IC9.47, R16.2
- net SEMC_D12: now also IC9.48, R15.2
- net SEMC_D13: now also IC9.50, R14.2
- net SEMC_D14: now also IC9.51, R13.2
- net SEMC_D15: now also IC9.53, R12.2
- net SEMC_D2: now also IC9.5, R35.1
- net SEMC_D3: now also IC9.7, R36.1
- net SEMC_D4: now also IC9.8, R37.1
- net SEMC_D5: now also IC9.10, R38.1
- net SEMC_D6: now also IC9.11, R39.1
- net SEMC_D7: now also IC9.13, R40.1
- net SEMC_D8: now also IC9.42, R19.2
- net SEMC_D9: now also IC9.44, R18.2
- net SEMC_DM0: now also IC9.15, R41.1
- net SEMC_DM1: now also IC9.39, R20.2
- net SEMC_RAS: now also IC9.18, R44.1
- net SEMC_WE: now also IC9.16, R42.1
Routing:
- net 3V3_BUS: track 486.1 -> 122.6 mm, vias 17 -> 33
- net NVCC_GPIO_3V3: track 134.6 -> 0.00 mm, vias 8 -> 0
- net GND: track 236.1 -> 109.4 mm, vias 57 -> 352
- net SDRAM_3V3: track 112.3 -> 58.4 mm, vias 8 -> 7
- net SEMC_D0: track 11.3 -> 64.4 mm
- net SEMC_D1: track 8.50 -> 61.5 mm
- net N$2: track 52.2 -> 0.00 mm
- net N$5: track 52.0 -> 0.00 mm
- net SEMC_D4: track 9.12 -> 55.4 mm
- net SEMC_D3: track 11.5 -> 57.0 mm
- net N$9: track 45.3 -> 0.00 mm
- net N$8: track 44.5 -> 0.00 mm
- net SEMC_D2: track 14.9 -> 59.3 mm
- net N$6: track 43.4 -> 0.00 mm
- net SEMC_D7: track 8.78 -> 48.0 mm
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- added copper zone on layer 1, net GND
- removed copper zone on layer 1, net NA_SIG
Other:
- board text added: "5V"
- board text added: "BIG"
- board text added: "BRAIN"
- board text added: "CDH TEAM"
- board text added: "FLASH"
- board text added: "GND"
- board text added: "HW: JONATHAN CASAMAYOR"
- board text added: "JTAG"
- board text added: "OBC"
- board text added: "REV. 0"
- board text added: "SDRAM"
- board text added: "SOC-i"
- board text added: "UW AACT"
